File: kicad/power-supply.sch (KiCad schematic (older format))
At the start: 22 parts, among them P1 BATTERY, Q1 MMBT3904, U1 MCP73832, U2 TPS62736

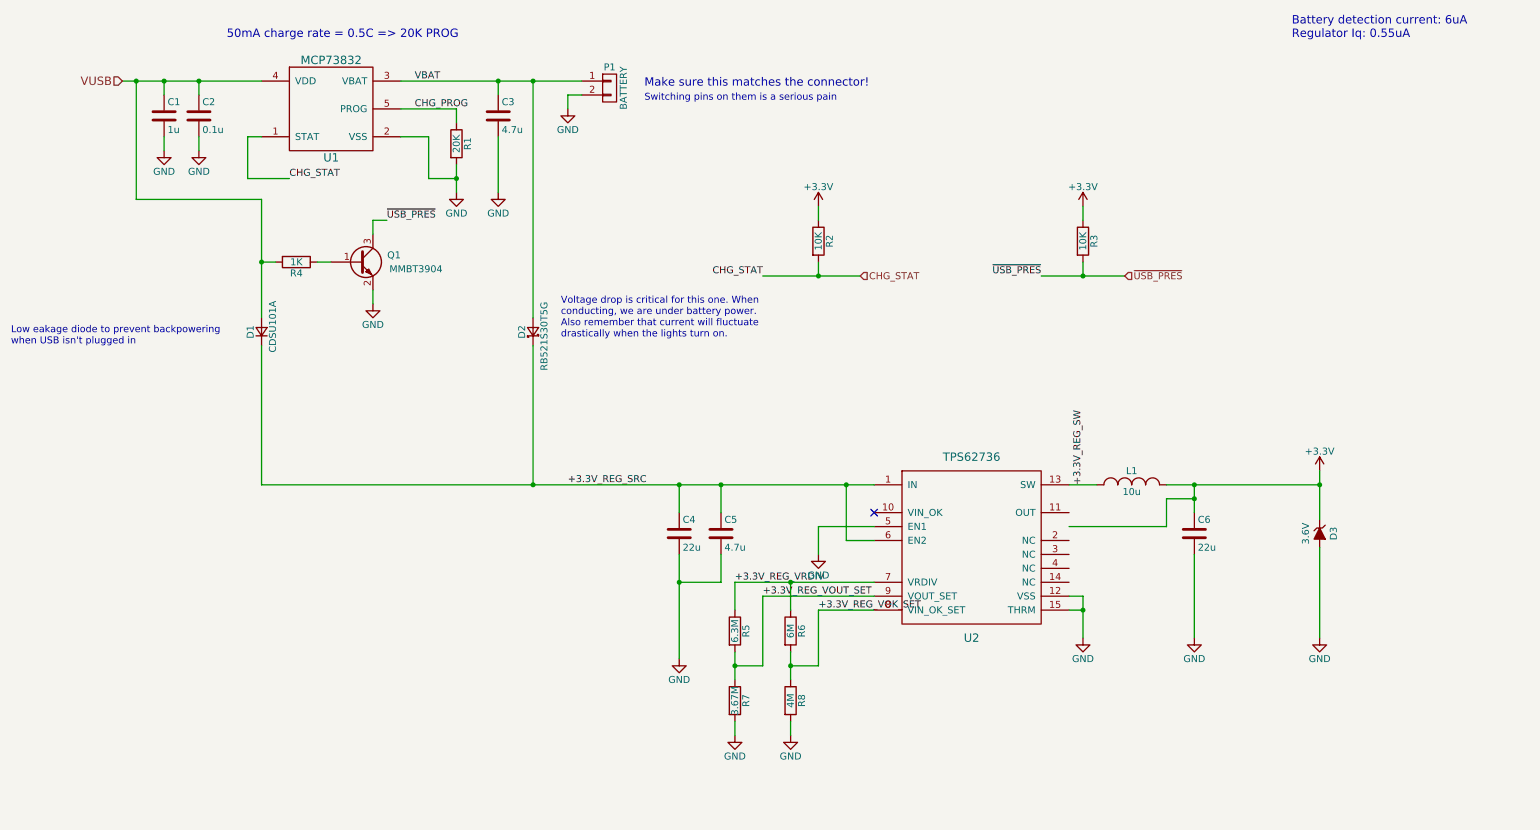
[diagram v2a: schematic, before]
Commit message: Finished initial placement of all components
Got rid of several pullup resistors and unnecessary components.
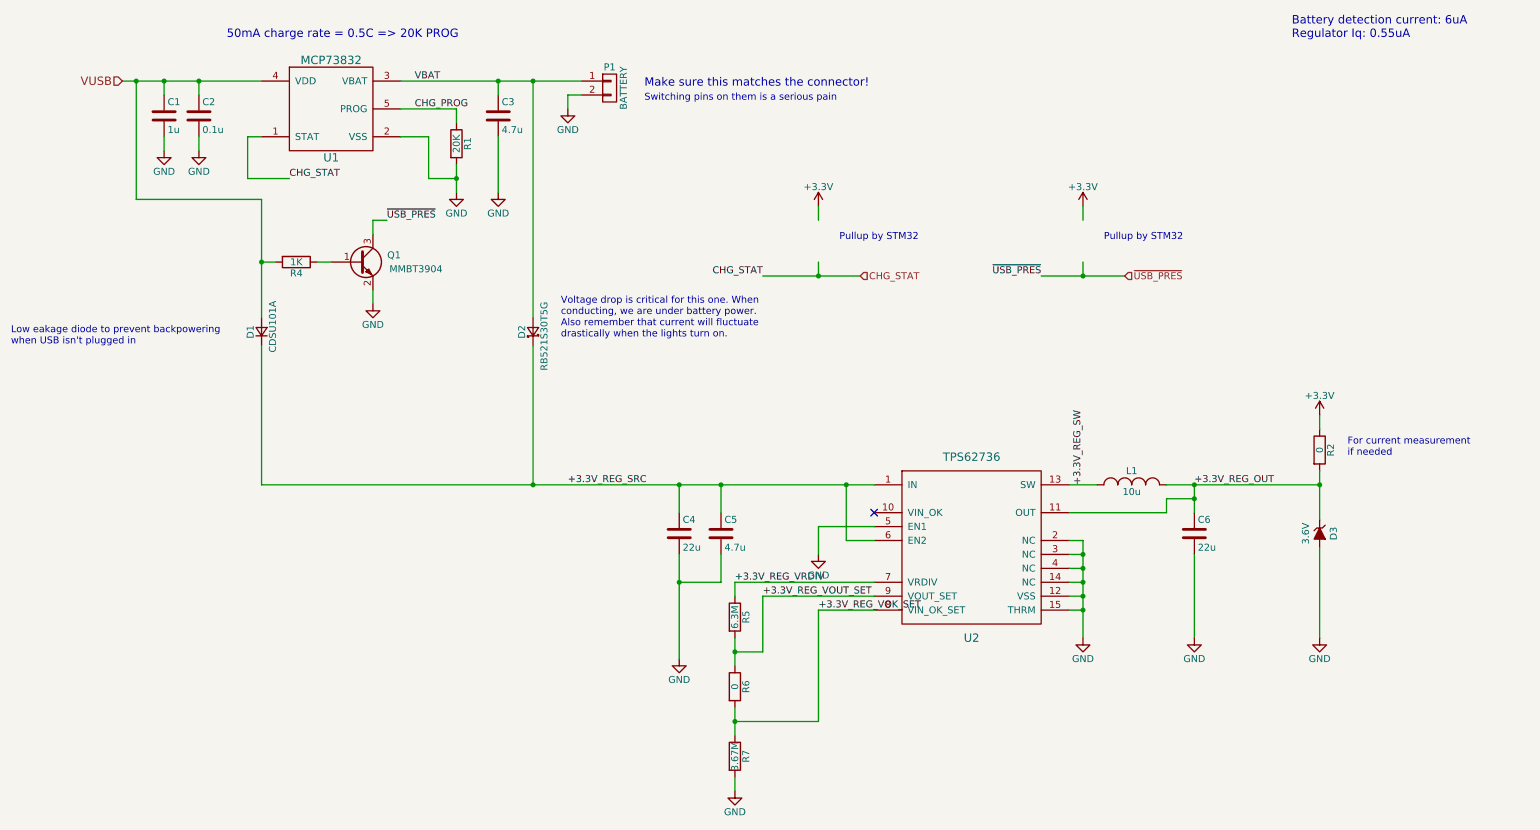
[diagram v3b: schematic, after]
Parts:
- removed R3: 10K, Resistors_SMD:R_0402, symbol R
- removed R8: 4M, Resistors_SMD:R_0402, symbol R
- R2: value 10K -> 0
- R6: value 6M -> 0
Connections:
- net labels added: +3.3V_REG_OUT
- wire segments 71 -> 74
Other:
- note added: "For current measurement\nif needed"
- note added: "Pullup by STM32"
- moved on the sheet: R5, R6, R7
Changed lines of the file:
@@
 L +3.3V #PWR09
 U 1 1 57FC5A4F
-P 9900 4100
-F 0 "#PWR09" H 9900 3950 50  0001 C CNN
-F 1 "+3.3V" H 9900 4240 50  0000 C CNN
-F 2 "" H 9900 4100 50  0000 C CNN
-F 3 "" H 9900 4100 50  0000 C CNN
-	1    9900 4100
+P 9900 3700
+F 0 "#PWR09" H 9900 3550 50  0001 C CNN
+F 1 "+3.3V" H 9900 3840 50  0000 C CNN
+F 2 "" H 9900 3700 50  0000 C CNN
+F 3 "" H 9900 3700 50  0000 C CNN
+	1    9900 3700
 	1    0    0    -1
 $EndComp
@@
 L R R5
 U 1 1 57FC6198
-P 5700 5250
-F 0 "R5" V 5780 5250 50  0000 C CNN
-F 1 "6.3M" V 5700 5250 50  0000 C CNN
-F 2 "Resistors_SMD:R_0402" V 5630 5250 50  0001 C CNN
-F 3 "" H 5700 5250 50  0000 C CNN
-	1    5700 5250
+P 5700 5150
+F 0 "R5" V 5780 5150 50  0000 C CNN
+F 1 "6.3M" V 5700 5150 50  0000 C CNN
+F 2 "Resistors_SMD:R_0402" V 5630 5150 50  0001 C CNN
+F 3 "" H 5700 5150 50  0000 C CNN
+	1    5700 5150
 	1    0    0    -1
 $EndComp
@@
 L R R7
 U 1 1 57FC6243
-P 5700 5750
-F 0 "R7" V 5780 5750 50  0000 C CNN
-F 1 "3.67M" V 5700 5750 50  0000 C CNN
-F 2 "Resistors_SMD:R_0402" V 5630 5750 50  0001 C CNN
-F 3 "" H 5700 5750 50  0000 C CNN
-	1    5700 5750
+P 5700 6150
+F 0 "R7" V 5780 6150 50  0000 C CNN
+F 1 "3.67M" V 5700 6150 50  0000 C CNN
+F 2 "Resistors_SMD:R_0402" V 5630 6150 50  0001 C CNN
+F 3 "" H 5700 6150 50  0000 C CNN
+	1    5700 6150
 	1    0    0    -1
 $EndComp
@@
 L GND #PWR011
 U 1 1 57FC6553
-P 5700 6000
-F 0 "#PWR011" H 5700 5750 50  0001 C CNN
-F 1 "GND" H 5700 5850 50  0000 C CNN
-F 2 "" H 5700 6000 50  0000 C CNN
-F 3 "" H 5700 6000 50  0000 C CNN
-	1    5700 6000
+P 5700 6400
+F 0 "#PWR011" H 5700 6150 50  0001 C CNN
+F 1 "GND" H 5700 6250 50  0000 C CNN
+F 2 "" H 5700 6400 50  0000 C CNN
+F 3 "" H 5700 6400 50  0000 C CNN
+	1    5700 6400
 	1    0    0    -1
 $EndComp
@@
 L R R6
 U 1 1 57FC6B32
-P 6100 5250
-F 0 "R6" V 6180 5250 50  0000 C CNN
-F 1 "6M" V 6100 5250 50  0000 C CNN
-F 2 "Resistors_SMD:R_0402" V 6030 5250 50  0001 C CNN
-F 3 "" H 6100 5250 50  0000 C CNN
-	1    6100 5250
-	1    0    0    -1
-$EndComp
-$Comp
-L R R8
-U 1 1 57FC6CCE
-P 6100 5750
-F 0 "R8" V 6180 5750 50  0000 C CNN
-F 1 "4M" V 6100 5750 50  0000 C CNN
-F 2 "Resistors_SMD:R_0402" V 6030 5750 50  0001 C CNN
-F 3 "" H 6100 5750 50  0000 C CNN
-	1    6100 5750
+P 5700 5650
+F 0 "R6" V 5780 5650 50  0000 C CNN
+F 1 "0" V 5700 5650 50  0000 C CNN
+F 2 "Resistors_SMD:R_0402" V 5630 5650 50  0001 C CNN
+F 3 "" H 5700 5650 50  0000 C CNN
+	1    5700 5650
 	1    0    0    -1
 $EndComp
 $Comp
 L GND #PWR012
-U 1 1 57FC6D09
-P 6100 6000
-F 0 "#PWR012" H 6100 5750 50  0001 C CNN
-F 1 "GND" H 6100 5850 50  0000 C CNN
-F 2 "" H 6100 6000 50  0000 C CNN
-F 3 "" H 6100 6000 50  0000 C CNN
-	1    6100 6000
-	1    0    0    -1
-$EndComp
-$Comp
-L GND #PWR013
 U 1 1 57FC72B8
 P 6300 4700
-F 0 "#PWR013" H 6300 4450 50  0001 C CNN
+F 0 "#PWR012" H 6300 4450 50  0001 C CNN
 F 1 "GND" H 6300 4550 50  0000 C CNN
 F 2 "" H 6300 4700 50  0000 C CNN
@@
 NoConn ~ 6700 4400
 $Comp
-L R R2
-U 1 1 57FC7B97
-P 6300 2450
-F 0 "R2" V 6380 2450 50  0000 C CNN
-F 1 "10K" V 6300 2450 50  0000 C CNN
-F 2 "Resistors_SMD:R_0402" V 6230 2450 50  0001 C CNN
-F 3 "" H 6300 2450 50  0000 C CNN
-	1    6300 2450
-	1    0    0    -1
-$EndComp
-$Comp
-L +3.3V #PWR014
+L +3.3V #PWR013
 U 1 1 57FC7C6B
 P 6300 2200
-F 0 "#PWR014" H 6300 2050 50  0001 C CNN
+F 0 "#PWR013" H 6300 2050 50  0001 C CNN
 F 1 "+3.3V" H 6300 2340 50  0000 C CNN
 F 2 "" H 6300 2200 50  0000 C CNN
@@
 CHG_STAT
 $Comp
-L +3.3V #PWR015
+L +3.3V #PWR014
 U 1 1 57FC80A3
 P 8200 2200
-F 0 "#PWR015" H 8200 2050 50  0001 C CNN
+F 0 "#PWR014" H 8200 2050 50  0001 C CNN
 F 1 "+3.3V" H 8200 2340 50  0000 C CNN
 F 2 "" H 8200 2200 50  0000 C CNN
 F 3 "" H 8200 2200 50  0000 C CNN
 	1    8200 2200
-	1    0    0    -1
-$EndComp
-$Comp
-L R R3
-U 1 1 57FC8129
-P 8200 2450
-F 0 "R3" V 8280 2450 50  0000 C CNN
-F 1 "10K" V 8200 2450 50  0000 C CNN
-F 2 "Resistors_SMD:R_0402" V 8130 2450 50  0001 C CNN
-F 3 "" H 8200 2450 50  0000 C CNN
-	1    8200 2450
 	1    0    0    -1
 $EndComp
@@
 $EndComp
 $Comp
-L GND #PWR016
+L GND #PWR015
 U 1 1 57FC84EA
 P 3100 2900
-F 0 "#PWR016" H 3100 2650 50  0001 C CNN
+F 0 "#PWR015" H 3100 2650 50  0001 C CNN
 F 1 "GND" H 3100 2750 50  0000 C CNN
 F 2 "" H 3100 2900 50  0000 C CNN
@@
 	9000 4200 9000 4400
 Wire Wire Line
-	8100 4500 8800 4500
-Wire Wire Line
-	8800 4500 8800 4300
+	8100 4400 8800 4400
+Wire Wire Line
+	8800 4400 8800 4300
 Wire Wire Line
 	8800 4300 9000 4300
 Connection ~ 9000 4300
 Wire Wire Line
-	8200 5000 8200 5300
+	8200 4600 8200 5300
 Wire Wire Line
 	8200 5000 8100 5000
@@
 	5700 4900 6700 4900
 Wire Wire Line
-	5700 4900 5700 5100
-Wire Wire Line
-	5700 5400 5700 5600
-Wire Wire Line
-	5700 5500 5900 5500
-Wire Wire Line
-	5900 5500 5900 5000
+	5700 4900 5700 5000
 Wire Wire Line
 	5900 5000 6700 5000
-Connection ~ 5700 5500
-Wire Wire Line
-	5700 6000 5700 5900
-Wire Wire Line
-	6100 5100 6100 4900
-Connection ~ 6100 4900
-Wire Wire Line
-	6100 6000 6100 5900
-Wire Wire Line
-	6100 5400 6100 5600
-Wire Wire Line
-	6100 5500 6300 5500
-Wire Wire Line
-	6300 5500 6300 5100
+Wire Wire Line
+	5700 6400 5700 6300
 Wire Wire Line
 	6300 5100 6700 5100
-Connection ~ 6100 5500
 Wire Wire Line
 	6700 4500 6300 4500
@@
 Wire Wire Line
 	8200 2300 8200 2200
+Text Notes 6450 2450 0    50   ~ 0
+Pullup by STM32
+Text Notes 8350 2450 0    50   ~ 0
+Pullup by STM32
+$Comp
+L R R2
+U 1 1 5804A98B
+P 9900 3950
+F 0 "R2" V 9980 3950 50  0000 C CNN
+F 1 "0" V 9900 3950 50  0000 C CNN
+F 2 "Resistors_SMD:R_0402" V 9830 3950 50  0001 C CNN
+F 3 "" H 9900 3950 50  0000 C CNN
+	1    9900 3950
+	1    0    0    -1
+$EndComp
+Wire Wire Line
+	9900 3700 9900 3800
+Text Notes 10100 4000 0    50   ~ 0
+For current measurement\nif needed
+Text Label 9000 4200 0    50   ~ 0
++3.3V_REG_OUT
+Wire Wire Line
+	8100 4600 8200 4600
+Connection ~ 8200 5000
+Wire Wire Line
+	8100 4900 8200 4900
+Connection ~ 8200 4900
+Wire Wire Line
+	8100 4800 8200 4800
+Connection ~ 8200 4800
+Wire Wire Line
+	8100 4700 8200 4700
+Connection ~ 8200 4700
+Wire Wire Line
+	5700 6000 5700 5800
+Wire Wire Line
+	5700 5500 5700 5300
+Wire Wire Line
+	5700 5400 5900 5400
+Wire Wire Line
+	5900 5400 5900 5000
+Connection ~ 5700 5400
+Wire Wire Line
+	6300 5100 6300 5900
+Wire Wire Line
+	6300 5900 5700 5900
+Connection ~ 5700 5900
 $EndSCHEMATC

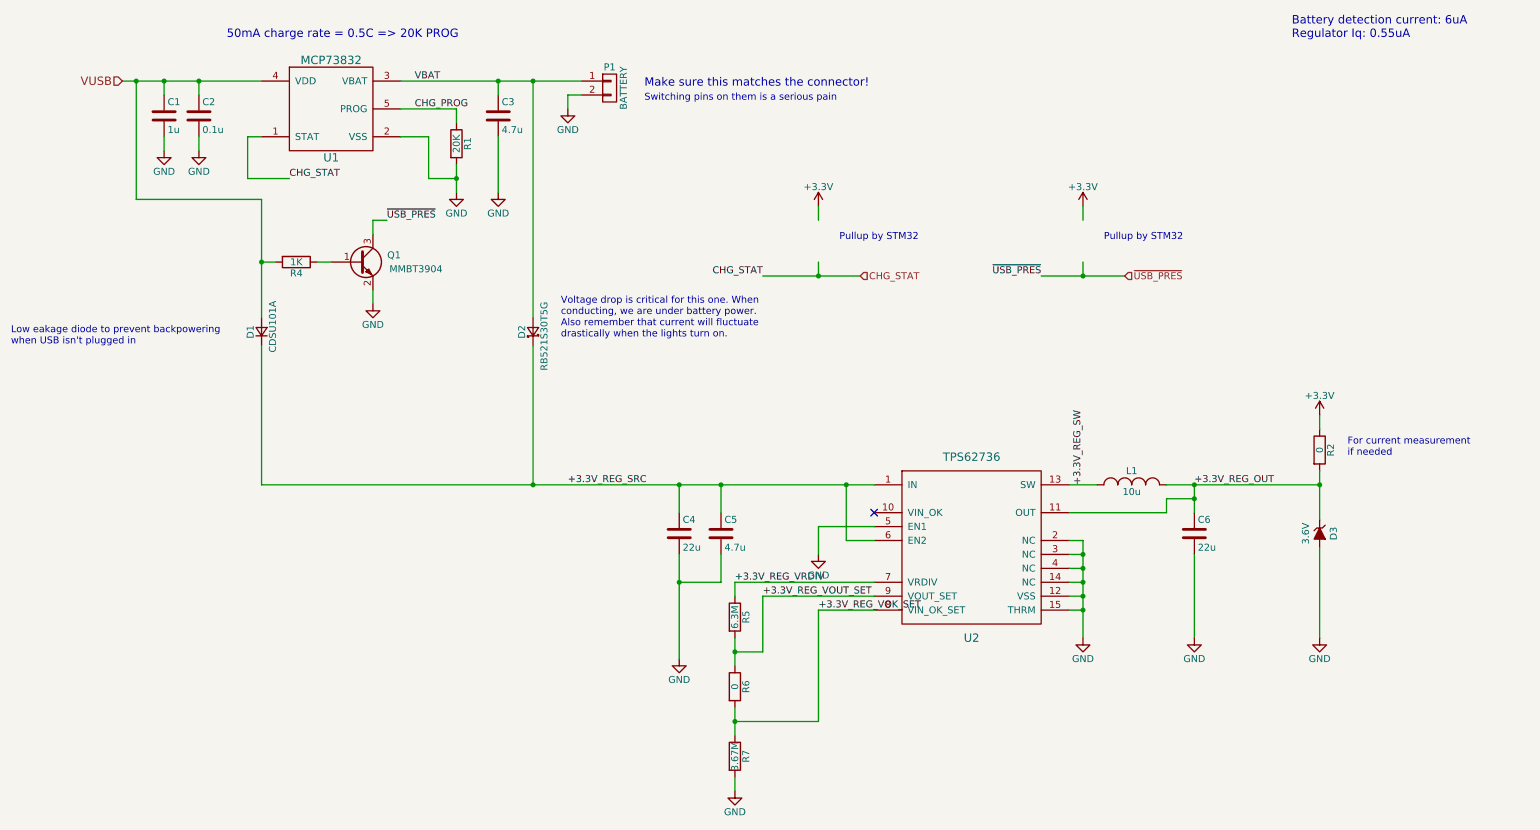
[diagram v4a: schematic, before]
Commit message: Checked layout and reference designs, swapped crystal and RGB LED
ST has a list of suggested crystals which are known to work with the
STM32L0 family. I selected one of those and it is significantly
smaller in all dimensions.

The RGB LED had too high of a green voltage. I swapped it out for a
slightly more expensive one with the same footprint that had startlingly
low green and blue forward voltages.

For layout changes:
- Fixed regulator footprint silkscreen
- Fixed regulator layout to be closer to reference design
- Fixed inductor silkscreen
- Moved accelerometer downward to accomodate capacitors above
- Fixed accelerometer layout to have no traces beneath
- Fixed accelerometer silkscreen
- Fixed LED silkscreen
- General small silkscreen edits, such as shifting text around

I've also chosen parts and values for all resistors and capacitors.
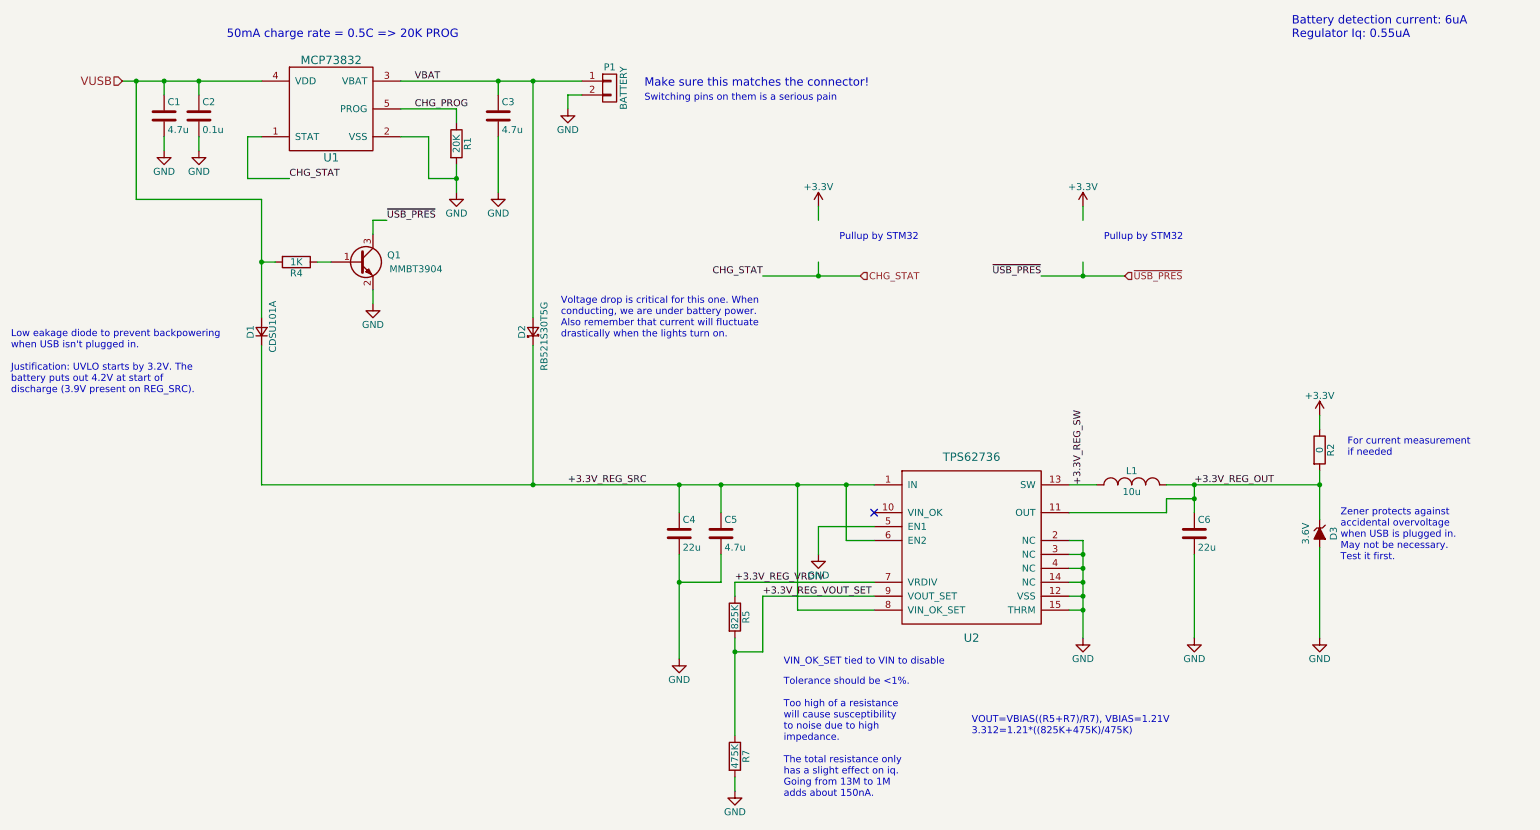
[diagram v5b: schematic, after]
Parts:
- removed R6: 0, Resistors_SMD:R_0402, symbol R
- C1: value 1u -> 4.7u; Part No. 1276-1448-1-ND -> 1276-6819-1-ND
- R1: Part No. (none) -> 311-20.0KLRCT-ND
- R2: Part No. (none) -> 311-0.0JRCT-ND
- R4: Part No. (none) -> 311-1.00KLRCT-ND
- R5: value 6.3M -> 825K; Part No. (none) -> YAG3241CT-ND
- R7: value 3.67M -> 475K; Part No. (none) -> 311-475KLRCT-ND
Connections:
- net labels removed: +3.3V_REG_VOK_SET
- wire segments 74 -> 72
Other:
- note added: "Low eakage diode to prevent backpowering\nwhen USB isn't plugged in.\n\nJustification: UVLO starts by 3.2V. The\nbattery puts out 4.2V at start of\ndischarge (3.9V present on REG_SRC)."
- note added: "Tolerance should be <1%.\n\nToo high of a resistance\nwill cause susceptibility\nto noise due to high\nimpedance.\n\nThe total resistance only\nhas a slight effect on iq.\nGoing from 13M to 1M\nadds about 150nA."
- note added: "VIN_OK_SET tied to VIN to disable"
- note added: "VOUT=VBIAS((R5+R7)/R7), VBIAS=1.21V\n3.312=1.21*((825K+475K)/475K)"
- note added: "Zener protects against\naccidental overvoltage\nwhen USB is plugged in.\nMay not be necessary.\nTest it first."
- note removed: "Low eakage diode to prevent backpowering\nwhen USB isn't plugged in"
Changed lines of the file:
@@
 F 2 "Resistors_SMD:R_0402" V 3630 1750 50  0001 C CNN
 F 3 "" H 3700 1750 50  0000 C CNN
+F 4 "311-20.0KLRCT-ND" H 3700 1750 60  0001 C CNN "Part No."
 	1    3700 1750
 	1    0    0    -1
@@
 P 1600 1550
 F 0 "C1" H 1625 1650 50  0000 L CNN
-F 1 "1u" H 1625 1450 50  0000 L CNN
+F 1 "4.7u" H 1625 1450 50  0000 L CNN
 F 2 "Capacitors_SMD:C_0402" H 1638 1400 50  0001 C CNN
 F 3 "" H 1600 1550 50  0000 C CNN
-F 4 "1276-1448-1-ND" H 1600 1550 60  0001 C CNN "Part No."
+F 4 "1276-6819-1-ND" H 1600 1550 60  0001 C CNN "Part No."
 	1    1600 1550
 	1    0    0    -1
@@
 	0    -1   -1   0
 $EndComp
-Text Notes 500  3200 0    50   ~ 0
-Low eakage diode to prevent backpowering\nwhen USB isn't plugged in
+Text Notes 500  3550 0    50   ~ 0
+Low eakage diode to prevent backpowering\nwhen USB isn't plugged in.\n\nJustification: UVLO starts by 3.2V. The\nbattery puts out 4.2V at start of\ndischarge (3.9V present on REG_SRC).
 $Comp
 L GND #PWR07
@@
 P 5700 5150
 F 0 "R5" V 5780 5150 50  0000 C CNN
-F 1 "6.3M" V 5700 5150 50  0000 C CNN
+F 1 "825K" V 5700 5150 50  0000 C CNN
 F 2 "Resistors_SMD:R_0402" V 5630 5150 50  0001 C CNN
 F 3 "" H 5700 5150 50  0000 C CNN
+F 4 "YAG3241CT-ND" H 5700 5150 60  0001 C CNN "Part No."
 	1    5700 5150
 	1    0    0    -1
@@
 P 5700 6150
 F 0 "R7" V 5780 6150 50  0000 C CNN
-F 1 "3.67M" V 5700 6150 50  0000 C CNN
+F 1 "475K" V 5700 6150 50  0000 C CNN
 F 2 "Resistors_SMD:R_0402" V 5630 6150 50  0001 C CNN
 F 3 "" H 5700 6150 50  0000 C CNN
+F 4 "311-475KLRCT-ND" H 5700 6150 60  0001 C CNN "Part No."
 	1    5700 6150
 	1    0    0    -1
@@
 $EndComp
 $Comp
-L R R6
-U 1 1 57FC6B32
-P 5700 5650
-F 0 "R6" V 5780 5650 50  0000 C CNN
-F 1 "0" V 5700 5650 50  0000 C CNN
-F 2 "Resistors_SMD:R_0402" V 5630 5650 50  0001 C CNN
-F 3 "" H 5700 5650 50  0000 C CNN
-	1    5700 5650
-	1    0    0    -1
-$EndComp
-$Comp
 L GND #PWR012
 U 1 1 57FC72B8
@@
 F 2 "Resistors_SMD:R_0402" V 2480 2600 50  0001 C CNN
 F 3 "" H 2550 2600 50  0000 C CNN
+F 4 "311-1.00KLRCT-ND" H 2550 2600 60  0001 C CNN "Part No."
 	1    2550 2600
 	0    1    1    0
@@
 Wire Wire Line
 	5700 6400 5700 6300
-Wire Wire Line
-	6300 5100 6700 5100
 Wire Wire Line
 	6700 4500 6300 4500
@@
 Text Label 5900 5000 0    50   ~ 0
 +3.3V_REG_VOUT_SET
-Text Label 6300 5100 0    50   ~ 0
-+3.3V_REG_VOK_SET
 Text Label 8200 4200 1    50   ~ 0
 +3.3V_REG_SW
@@
 F 2 "Resistors_SMD:R_0402" V 9830 3950 50  0001 C CNN
 F 3 "" H 9900 3950 50  0000 C CNN
+F 4 "311-0.0JRCT-ND" H 9900 3950 60  0001 C CNN "Part No."
 	1    9900 3950
 	1    0    0    -1
@@
 Connection ~ 8200 4700
 Wire Wire Line
-	5700 6000 5700 5800
-Wire Wire Line
-	5700 5500 5700 5300
+	5700 5300 5700 6000
 Wire Wire Line
 	5700 5400 5900 5400
@@
 	5900 5400 5900 5000
 Connection ~ 5700 5400
-Wire Wire Line
-	6300 5100 6300 5900
-Wire Wire Line
-	6300 5900 5700 5900
-Connection ~ 5700 5900
+Text Notes 10050 4750 0    50   ~ 0
+Zener protects against\naccidental overvoltage\nwhen USB is plugged in.\nMay not be necessary.\nTest it first.
+Wire Wire Line
+	6700 5100 6150 5100
+Wire Wire Line
+	6150 5100 6150 4200
+Connection ~ 6150 4200
+Text Notes 6050 5500 0    50   ~ 0
+VIN_OK_SET tied to VIN to disable
+Text Notes 6050 6450 0    50   ~ 0
+Tolerance should be <1%.\n\nToo high of a resistance\nwill cause susceptibility\nto noise due to high\nimpedance.\n\nThe total resistance only\nhas a slight effect on iq.\nGoing from 13M to 1M\nadds about 150nA.
+Text Notes 7400 6000 0    50   ~ 0
+VOUT=VBIAS((R5+R7)/R7), VBIAS=1.21V\n3.312=1.21*((825K+475K)/475K)
 $EndSCHEMATC
